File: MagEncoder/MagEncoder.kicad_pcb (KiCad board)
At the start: 4 copper layers, 52.5 x 24.8 mm, 32 parts, among them J1 Main, J2 Debug, J3 Thermistor, U1 ADM4852, U2 STM32G4A1KEU4, U3 LP5907MFX-3.3, U4 MA730

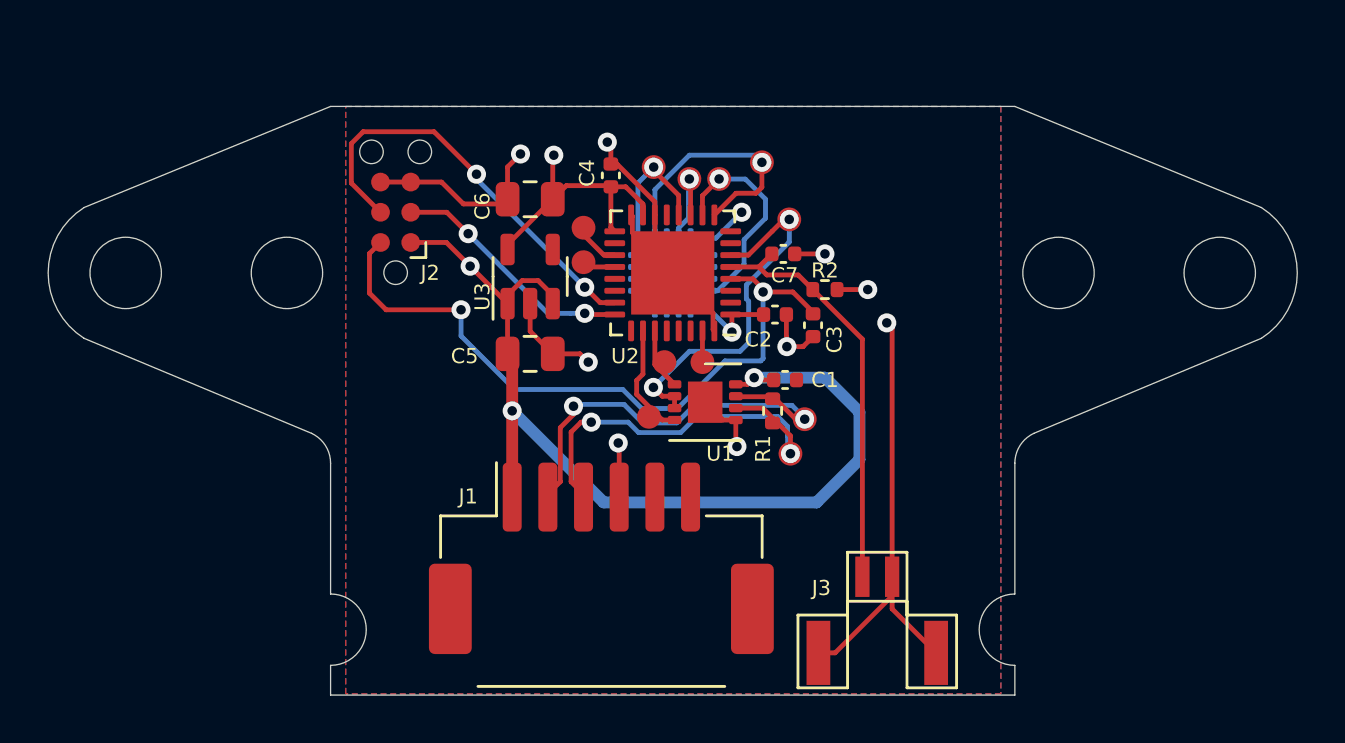
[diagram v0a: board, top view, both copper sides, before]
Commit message: Add RGB LED
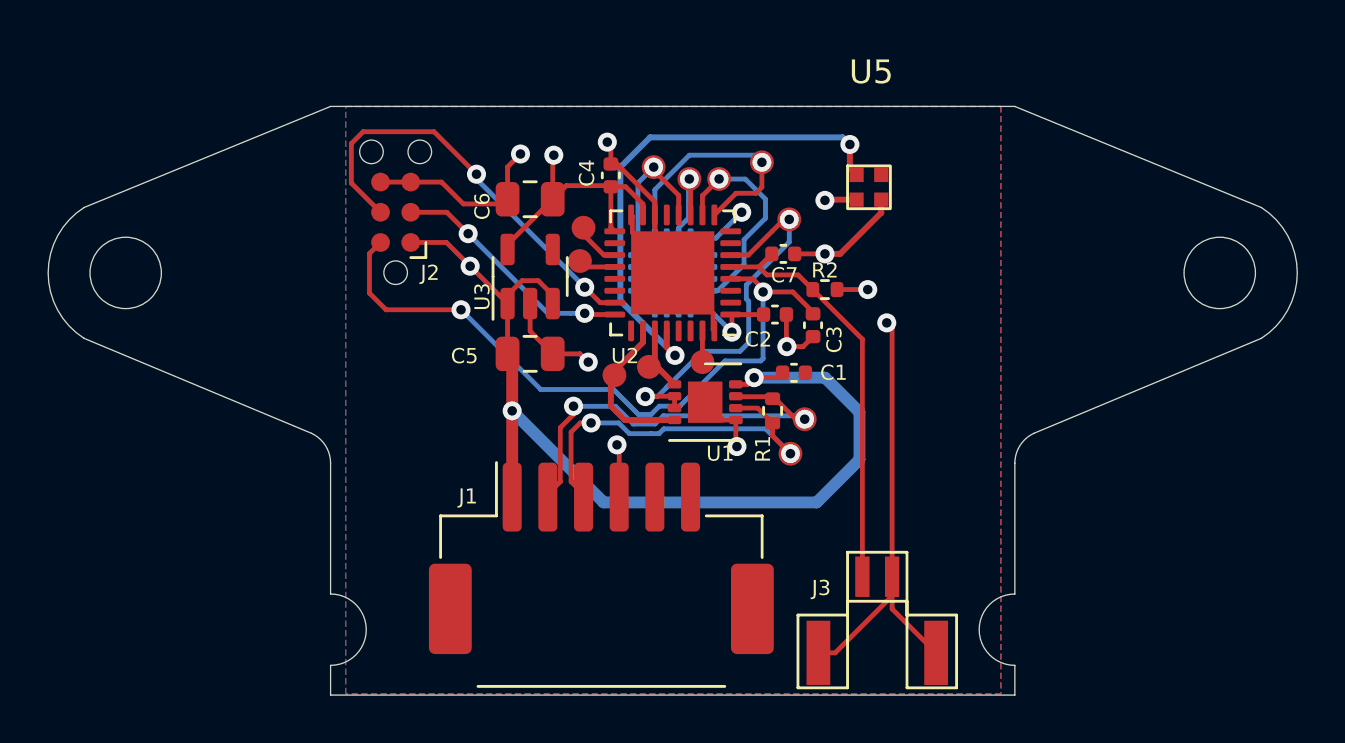
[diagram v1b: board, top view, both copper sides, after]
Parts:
- removed H3, H4: MountingHole, MountingHole:MountingHole_3mm
- added U5: LTST-E263CEGBK, ODrive_KiCad:LTST, F.Cu at (130.2, 64.4)
- moved TP5 2.27 mm to (119.5, 72.3)
- moved TP6 0.68 mm to (121.0, 72.0)
- moved C1 0.48 mm to (127.1, 72.2)
- moved TP3 0.16 mm to (118.1, 67.5)
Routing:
- net /I2S3_SD: track 0.00 -> 21.7 mm, vias 0 -> 2
- net GNDD: track 61.3 -> 63.3 mm
- net /USART2_TX: track 4.82 -> 6.64 mm
- net +5V: track 42.1 -> 43.8 mm, vias 3 -> 4
- net /RS485_P: track 17.5 -> 16.3 mm
- net /USART2_DE: track 15.4 -> 16.2 mm
